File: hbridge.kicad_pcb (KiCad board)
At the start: 2 copper layers, 27.9 x 37.1 mm, 28 parts, among them J11 Conn_01x06_Male, J12 Screw_Terminal_01x04, Q1 2N7000, Q11 2N7000, Q12 2N7000, Q13 2N3904, Q14 2N3906, Q15 2N3904, Q16 2N3906, Q17 STP20NF06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

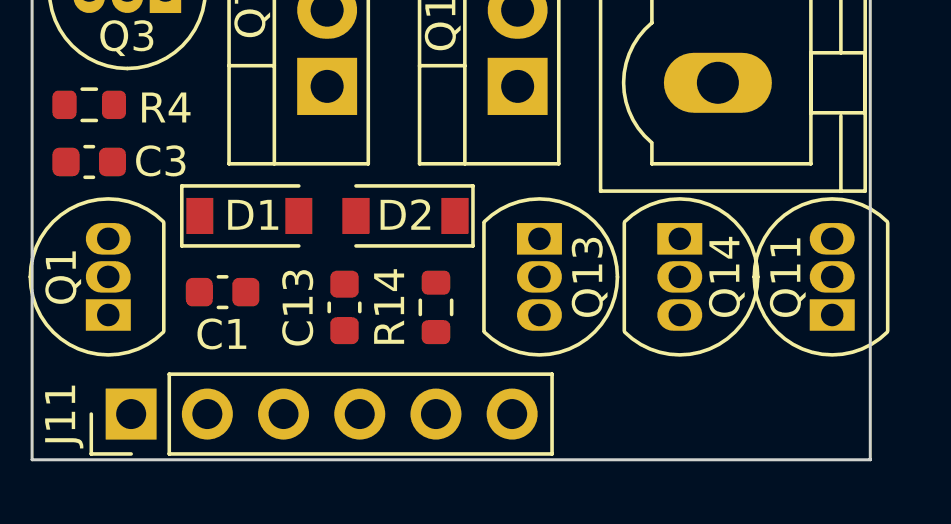
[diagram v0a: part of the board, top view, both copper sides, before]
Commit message: Switched out diodes for more common parts
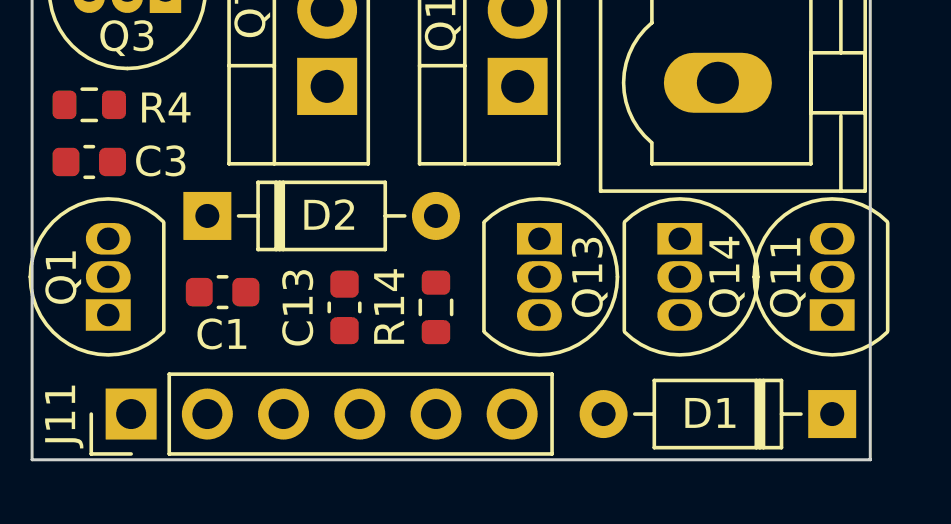
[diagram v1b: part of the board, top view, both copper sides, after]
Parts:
- D1, D2: value BAS116GWX -> 1N4148; footprint Diode_SMD:D_SOD-123 -> Diode_THT:D_DO-35_SOD27_P7.62mm_Horizontal
- moved D1 20.5 mm to (132.1, 90.9), turned to 180 degrees
- moved D2 6.60 mm to (111.3, 84.3), turned to 0 degrees

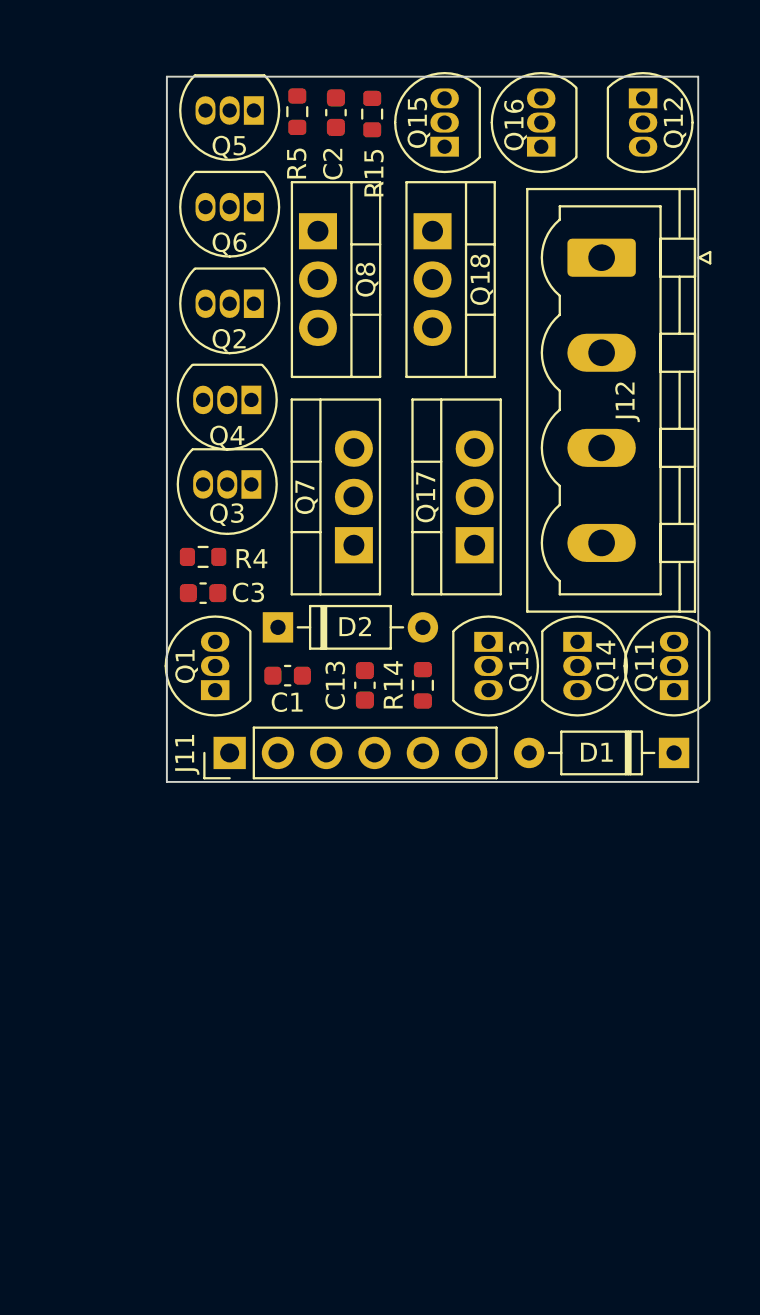
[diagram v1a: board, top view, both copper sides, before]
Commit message: Routed traces
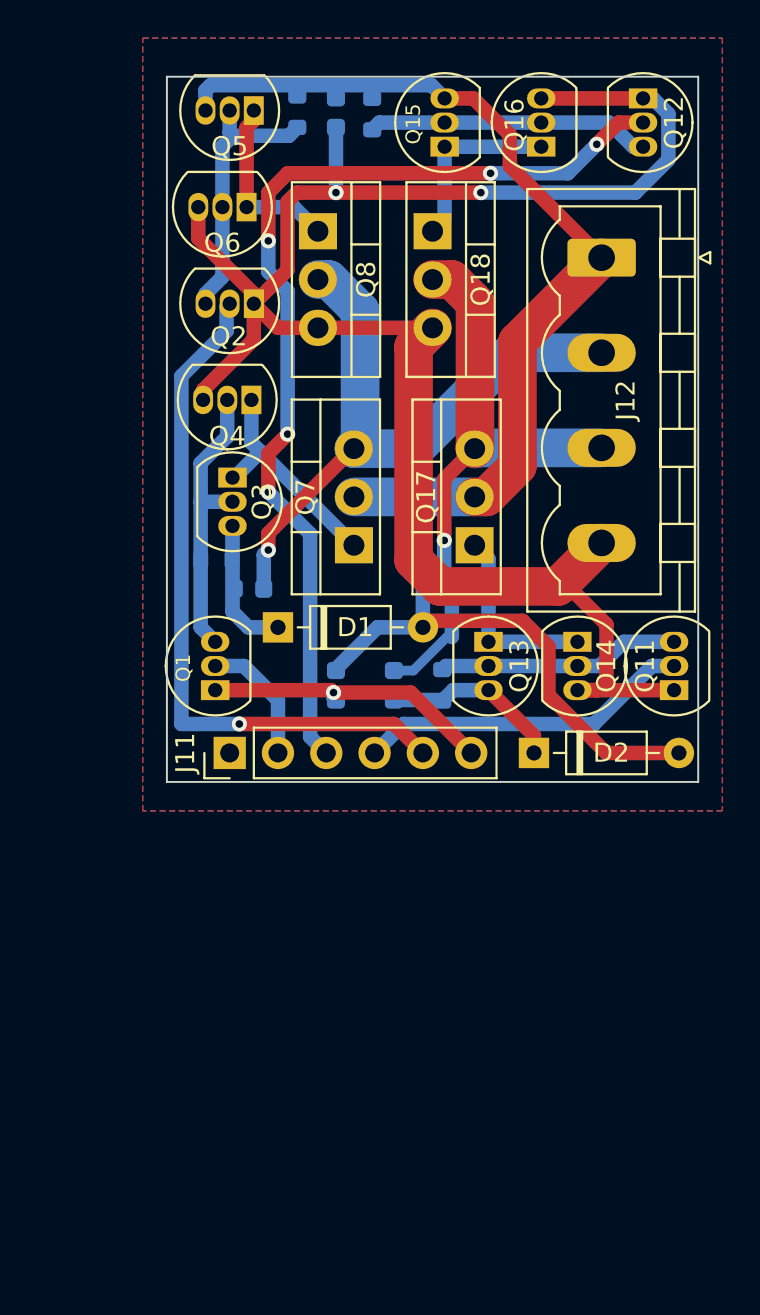
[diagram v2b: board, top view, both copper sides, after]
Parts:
- C1, C13, C2, C3, R14, R15, R4, R5: moved to B.Cu
- moved D1 21.8 mm to (111.3, 84.3), turned to 0 degrees
- moved D2 15.0 mm to (124.7, 90.9)
- moved C1 2.59 mm to (114.3, 87.4), turned to -90 degrees
- moved C3 2.42 mm to (109.7, 82.3)
- moved C13 1.52 mm to (117.3, 87.4), turned to 90 degrees
- moved Q3 1.06 mm to (108.9, 76.5), turned to -90 degrees
- moved R14 1.02 mm to (119.9, 87.4)
- moved R4 0.71 mm to (108.0, 80.8), turned to 180 degrees
- moved Q6 0.38 mm to (109.6, 62.2)
- turned R5 to -90 degrees
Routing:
- net GND: track 0.00 -> 114.7 mm, vias 0 -> 3
- net +12V: track 0.00 -> 79.3 mm
- net /L2: track 0.00 -> 52.8 mm, vias 0 -> 5
- net /L1: track 0.00 -> 36.5 mm, vias 0 -> 1
- net /OUT1: track 0.00 -> 34.7 mm, vias 0 -> 1
- net /OUT2: track 0.00 -> 31.6 mm, vias 0 -> 1
- net /H2: track 0.00 -> 17.6 mm
- net Net-(Q1-Pad3): track 0.00 -> 15.3 mm
- net Net-(Q12-Pad3): track 0.00 -> 14.9 mm
- net Net-(Q2-Pad3): track 0.00 -> 14.4 mm
- net Net-(Q11-Pad3): track 0.00 -> 12.8 mm
- net /drvH1: track 0.00 -> 11.9 mm
- net /drvH2: track 0.00 -> 10.1 mm
- net /drvL2: track 0.00 -> 9.79 mm
- net /boot2: track 0.00 -> 9.52 mm
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- added copper zone on B.Cu, net GND
- added copper zone on F.Cu, net GND

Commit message: Finished sikscreen
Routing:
- net GND: vias 3 -> 15
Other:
- board text added: "April 2022"
- board text added: "github.com/kamocat/hbridge"
- board text added: "hbridge v1.0"

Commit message: Finishing touches, sent off to fab
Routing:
- net GND: track 114.7 -> 118.3 mm
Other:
- board text added: "Gnd"
- board text added: "H1"
- board text added: "H2"
- board text added: "L1"
- board text added: "L2"
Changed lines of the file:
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@@
     (pad_to_mask_clearance 0)
     (pcbplotparams
-      (layerselection 0x00010fc_ffffffff)
+      (layerselection 0x00010f0_ffffffff)
       (disableapertmacros false)
       (usegerberextensions false)
@@
       (outputformat 1)
       (mirror false)
-      (drillshape 1)
+      (drillshape 0)
       (scaleselection 1)
-      (outputdirectory "")
+      (outputdirectory "gerbers/")
     )
   )
@@
     (effects (font (size 0.762 0.762) (thickness 0.127)) (justify mirror))
   )
+  (gr_text "H1" (at 111.252 89.408) (layer "B.SilkS")
+    (effects (font (size 0.762 0.762) (thickness 0.127)) (justify mirror))
+  )
+  (gr_text "H2" (at 116.332 89.408) (layer "B.SilkS")
+    (effects (font (size 0.762 0.762) (thickness 0.127)) (justify mirror))
+  )
+  (gr_text "Gnd" (at 121.412 89.408) (layer "B.SilkS")
+    (effects (font (size 0.762 0.762) (thickness 0.127)) (justify mirror))
+  )
+  (gr_text "L1" (at 118.872 89.408) (layer "B.SilkS")
+    (effects (font (size 0.762 0.762) (thickness 0.127)) (justify mirror))
+  )
+  (gr_text "L2" (at 113.792 89.408) (layer "B.SilkS")
+    (effects (font (size 0.762 0.762) (thickness 0.127)) (justify mirror))
+  )
   (gr_text "April 2022" (at 128.016 67.437) (layer "B.SilkS")
     (effects (font (size 0.762 0.762) (thickness 0.127)) (justify mirror))
+  )
+  (gr_text "L1" (at 118.872 88.9) (layer "F.SilkS")
+    (effects (font (size 0.762 0.762) (thickness 0.127)))
+  )
+  (gr_text "H1" (at 111.252 88.9) (layer "F.SilkS")
+    (effects (font (size 0.762 0.762) (thickness 0.127)))
+  )
+  (gr_text "H2" (at 116.332 88.9) (layer "F.SilkS")
+    (effects (font (size 0.762 0.762) (thickness 0.127)))
+  )
+  (gr_text "L2" (at 113.792 88.9) (layer "F.SilkS")
+    (effects (font (size 0.762 0.762) (thickness 0.127)))
   )
   (dimension (type aligned) (layer "Dwgs.User")
@@
   (segment (start 118.379997 69.580003) (end 119.38 68.58) (width 2.032) (layer "F.Cu") (net 2))
   (segment (start 107.95 87.63) (end 114.046 87.63) (width 0.762) (layer "F.Cu") (net 2))
+  (segment (start 126.365 90.805) (end 126.365 90.143223) (width 0.762) (layer "F.Cu") (net 2))
   (segment (start 119.770011 82.178011) (end 118.379997 80.787997) (width 2.032) (layer "F.Cu") (net 2))
+  (segment (start 126.365 90.143223) (end 124.3584 88.136623) (width 0.762) (layer "F.Cu") (net 2))
   (segment (start 128.27 79.89) (end 125.981989 82.178011) (width 2.032) (layer "F.Cu") (net 2))
   (segment (start 128.524 84.177978) (end 126.524033 82.178011) (width 0.762) (layer "F.Cu") (net 2))
@@
   (segment (start 109.982 66.791559) (end 109.982 67.31) (width 0.762) (layer "F.Cu") (net 2))
   (segment (start 112.235478 61.468) (end 114.3 61.468) (width 0.762) (layer "F.Cu") (net 2))
+  (segment (start 124.3584 88.136623) (end 124.3584 88.0364) (width 0.762) (layer "F.Cu") (net 2))
   (segment (start 107.315 71.850559) (end 107.315 72.369) (width 0.762) (layer "F.Cu") (net 2))
   (segment (start 114.046 87.63) (end 114.173 87.757) (width 0.762) (layer "F.Cu") (net 2))
@@
   (segment (start 108.86 78.994) (end 108.86 83.498) (width 0.762) (layer "B.Cu") (net 14))
   (segment (start 108.86 83.498) (end 109.69 84.328) (width 0.762) (layer "B.Cu") (net 14))
-  (segment (start 124.714 90.022) (end 122.322 87.63) (width 0.762) (layer "F.Cu") (net 15))
-  (segment (start 124.714 90.932) (end 124.714 90.022) (width 0.762) (layer "F.Cu") (net 15))
+  (segment (start 124.46 90.932) (end 122.322 88.794) (width 0.762) (layer "F.Cu") (net 15))
+  (segment (start 122.322 88.794) (end 122.322 87.63) (width 0.762) (layer "F.Cu") (net 15))
+  (segment (start 124.714 90.932) (end 124.46 90.932) (width 0.762) (layer "F.Cu") (net 15))
   (segment (start 120.459 87.63) (end 119.888 88.201) (width 0.762) (layer "B.Cu") (net 15))
   (segment (start 122.322 87.63) (end 120.459 87.63) (width 0.762) (layer "B.Cu") (net 15))

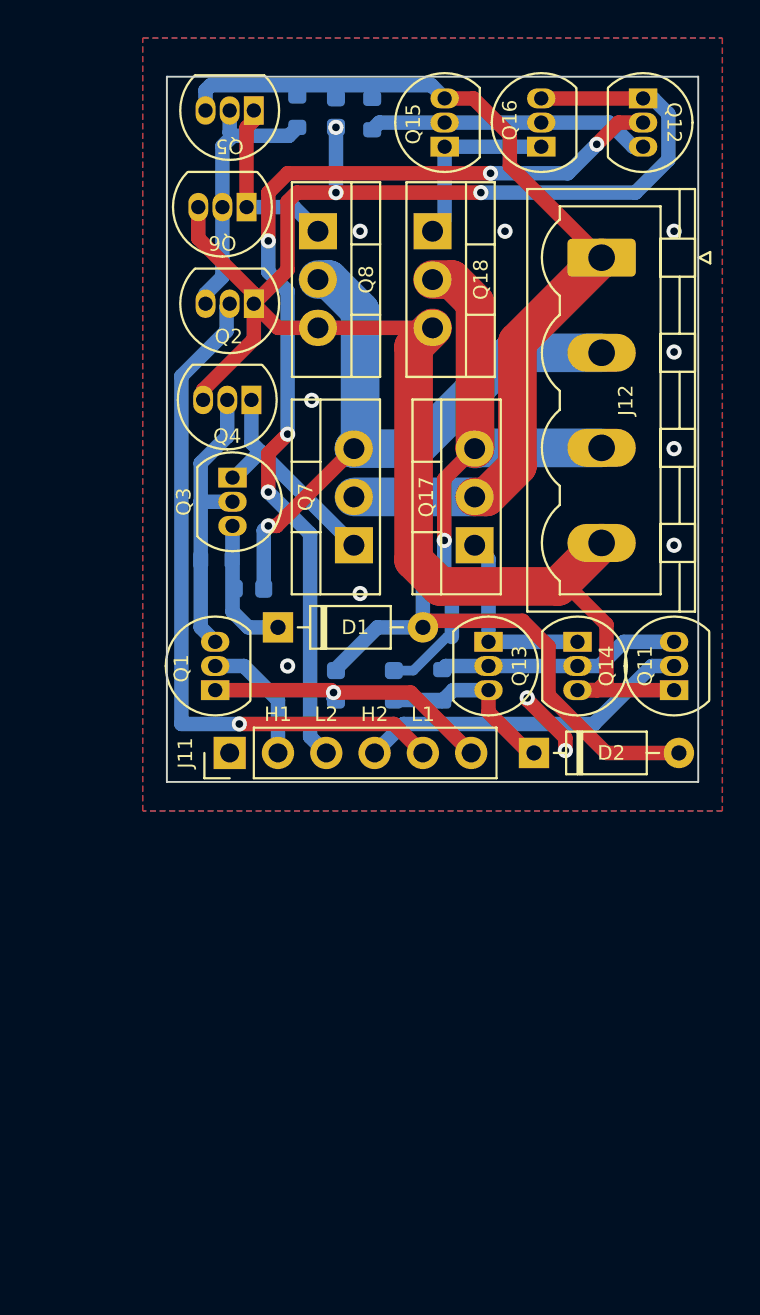
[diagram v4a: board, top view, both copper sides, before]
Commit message: Added logic to simplify control
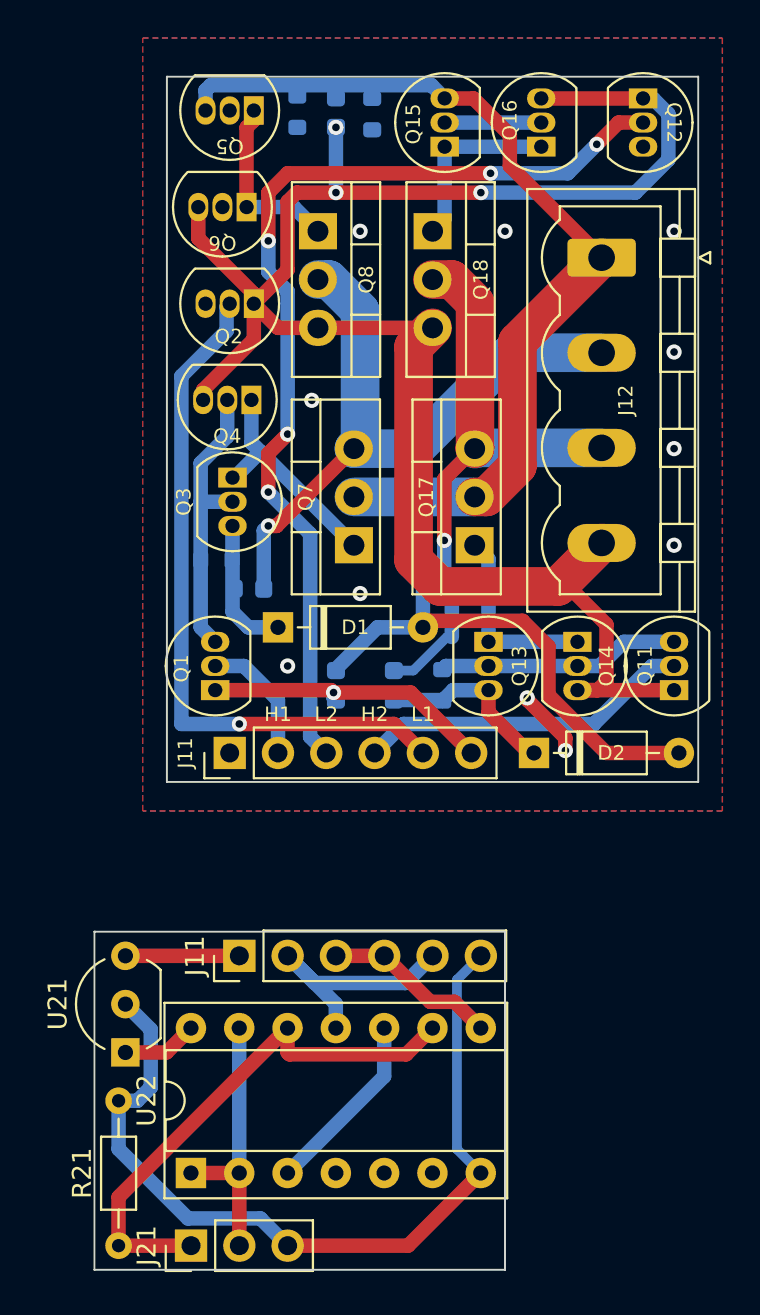
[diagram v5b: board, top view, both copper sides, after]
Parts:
- added J11: Conn_01x06_Male, Connector_PinHeader_2.54mm:PinHeader_1x06_P2.54mm_Vertical, F.Cu at (109.2, 101.6)
- added J21: Conn_01x03_Male, Connector_PinHeader_2.54mm:PinHeader_1x03_P2.54mm_Vertical, F.Cu at (106.7, 116.8)
- added R21: 10k, Resistor_THT:R_Axial_DIN0204_L3.6mm_D1.6mm_P7.62mm_Horizontal, F.Cu at (102.9, 116.8)
- added U21: LM78L05_TO92, Package_TO_SOT_THT:TO-92_Inline_Wide, F.Cu at (103.2, 106.7)
- added U22: 74HC00, Package_DIP:DIP-14_W7.62mm_Socket, F.Cu at (106.7, 113.0)
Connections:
- J11 pad 1: +5V -> +12V
- Q15 pad 2: Net-(Q12-Pad3) -> /H2
- Q16 pad 2: Net-(Q12-Pad3) -> /H2
- Q5 pad 2: Net-(Q2-Pad3) -> /H1
- Q6 pad 2: Net-(Q2-Pad3) -> /H1
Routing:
- net GND: track 118.3 -> 163.0 mm
- net /EN: track 0.00 -> 28.4 mm
- net Net-(Q12-Pad3): track 14.9 -> 0.00 mm
- net Net-(Q2-Pad3): track 14.4 -> 0.00 mm
- net /H2: track 17.6 -> 31.9 mm
- net /DIR: track 0.00 -> 14.0 mm
- net /H1: track 6.83 -> 20.5 mm
- net Net-(U22-Pad10): track 0.00 -> 9.72 mm
- net +12V: track 79.3 -> 85.3 mm
- net +5V: track 0.00 -> 3.98 mm
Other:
- board size 27.9 x 37.1 mm -> 31.8 x 62.7 mm

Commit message: Used internal layer to show redlines
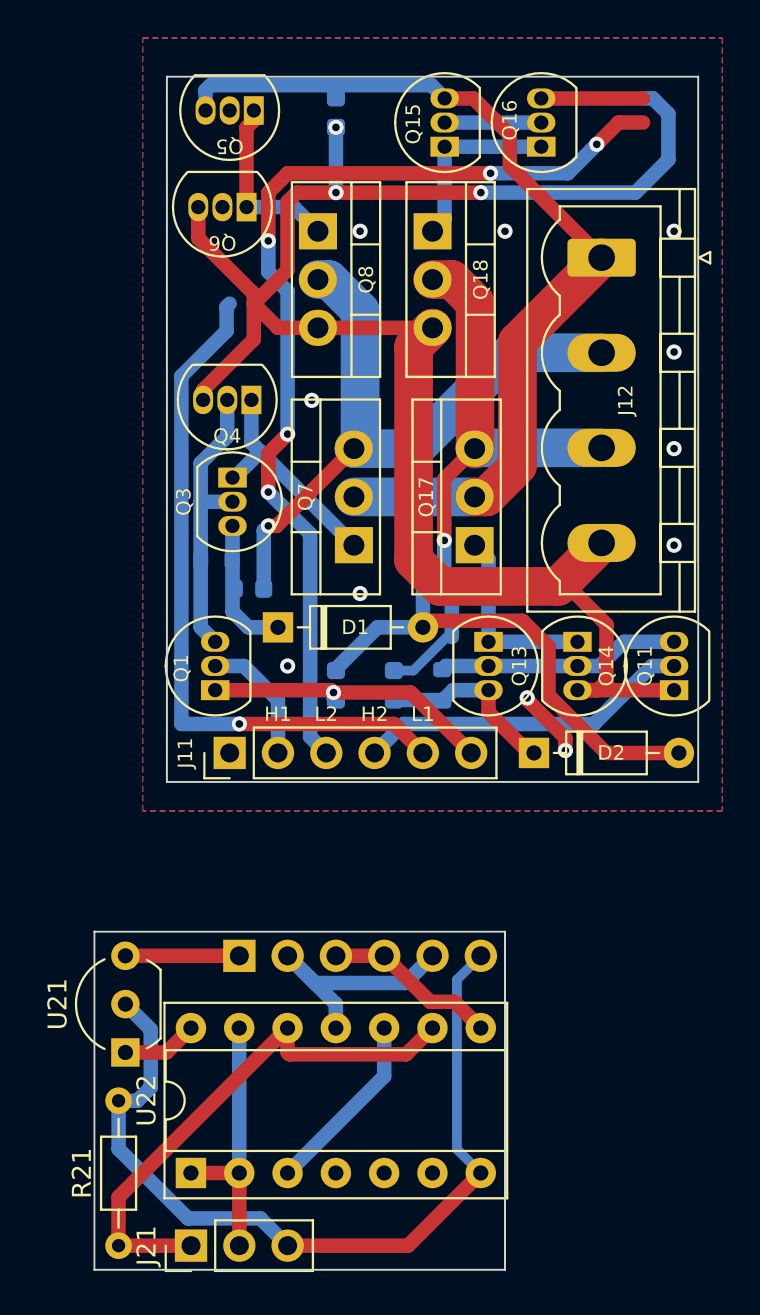
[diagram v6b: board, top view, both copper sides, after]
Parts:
- removed the J11 at (109.2, 101.6)
- removed Q12, Q2: 2N7000, Package_TO_SOT_THT:TO-92_Inline
- removed R15, R5: 10k, Resistor_SMD:R_0603_1608Metric
- added J22: Conn_01x06_Female, Connector_PinSocket_2.54mm:PinSocket_1x06_P2.54mm_Vertical, B.Cu at (109.2, 101.6)
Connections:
- J11 pad 3: /L2 -> /H2
- J11 pad 5: /L1 -> /H1
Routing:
- net /H2: track 31.9 -> 117.5 mm, vias 0 -> 5
- net /H1: track 20.5 -> 88.4 mm, vias 0 -> 1
- net /L2: track 52.8 -> 0.00 mm, vias 5 -> 0
- net /L1: track 36.5 -> 0.00 mm, vias 1 -> 0
- net +12V: track 85.3 -> 98.2 mm
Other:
- copper layers 2 -> 4
